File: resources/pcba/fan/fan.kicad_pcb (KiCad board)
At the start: 2 copper layers, 19 x 18 mm, 7 parts, among them Q1 PMOS 9301

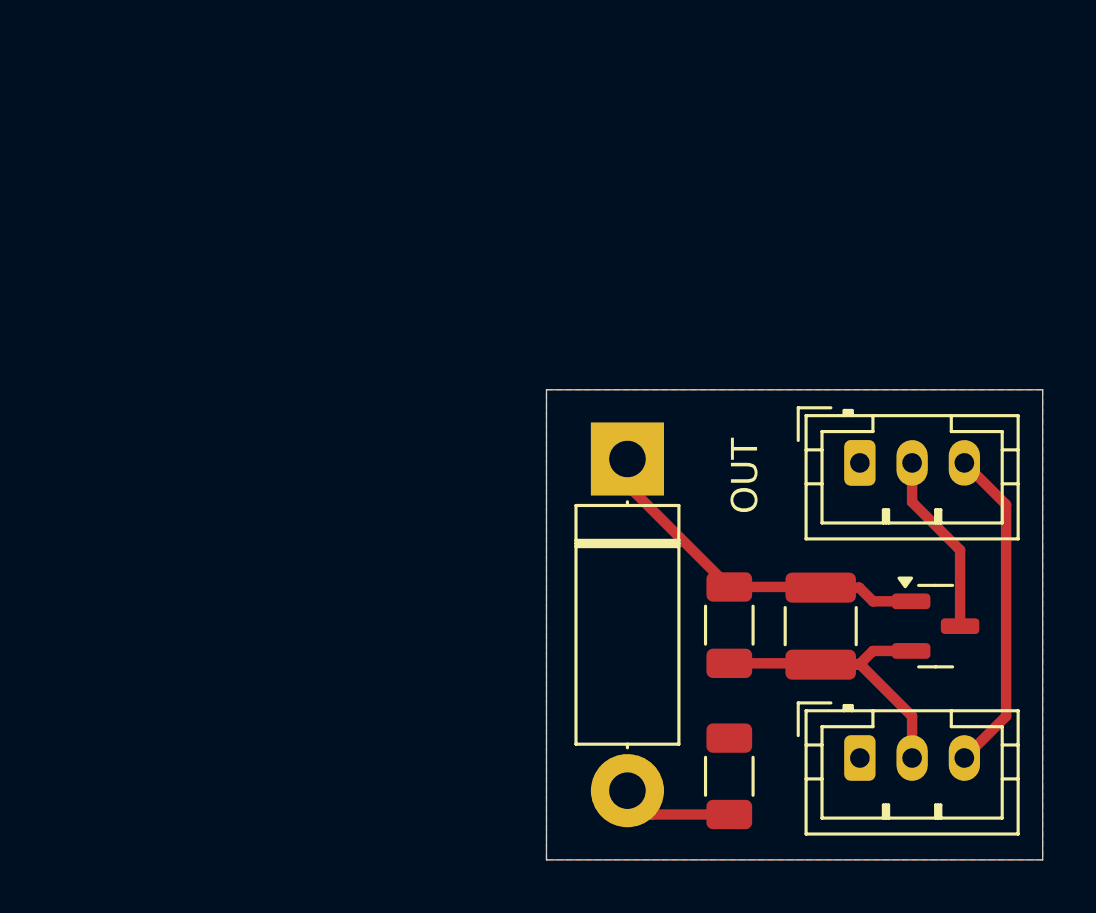
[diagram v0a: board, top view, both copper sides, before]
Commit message: add uvp and fan pcb
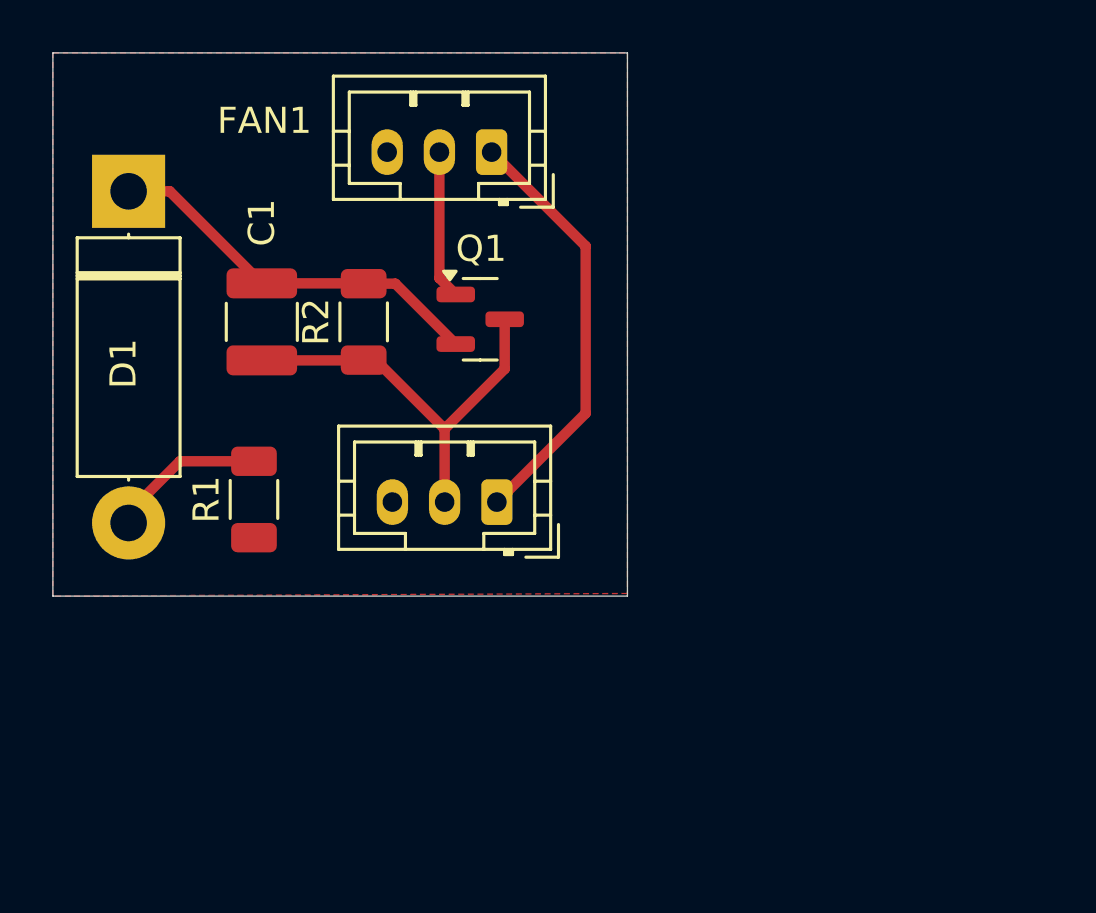
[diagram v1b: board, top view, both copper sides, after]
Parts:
- removed IN1: y1=0 y2=8 td=10m tr=1m tf=1m tw=100n per=10m, Connector_JST:JST_PH_B3B-PH-K_1x03_P2.00mm_Vertical
- removed IN2: OUT, Connector_JST:JST_PH_B3B-PH-K_1x03_P2.00mm_Vertical
- added FAN1: Conn_01x03_Socket, Connector_JST:JST_PH_B3B-PH-K_1x03_P2.00mm_Vertical, F.Cu at (124.9, 64.9)
- added INV1: Conn_01x03_Socket, Connector_JST:JST_PH_B3B-PH-K_1x03_P2.00mm_Vertical, F.Cu at (125.1, 78.3)
- C1: value 22uF -> 10u
- Q1: value PMOS 9301 -> PMOS
- R1: value 10k -> 1k
- R2: value 1k -> 10k
- moved C1 24.4 mm to (116.1, 71.4)
- moved R2 22.3 mm to (120.0, 71.4), turned to 90 degrees
- moved D1 21.7 mm to (111.0, 66.4)
- moved Q1 21.0 mm to (124.5, 71.3)
- moved R1 18.8 mm to (115.8, 78.2), turned to 90 degrees
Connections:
- C1 pad 2: +12V -> Net-(INV1-+)
- Q1 pad 1: Net-(D1-K) -> /FAN
- Q1 pad 2: +12V -> Net-(D1-K)
- Q1 pad 3: /FAN -> Net-(INV1-+)
- R1 pad 1: Net-(D1-K) -> GND
- R1 pad 2: +12V -> Net-(D1-A)
- R2 pad 1: GND -> Net-(INV1-+)
- R2 pad 2: Net-(D1-A) -> Net-(D1-K)
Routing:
- net Net-(INV1-+): track 0.00 -> 16.1 mm
- net +12V: track 13.0 -> 0.00 mm
- net /TACHOMETER: track 12.6 -> 16.3 mm
- net Net-(D1-A): track 4.28 -> 6.01 mm
- net /FAN: track 7.01 -> 5.71 mm
- net Net-(D1-K): track 13.8 -> 14.9 mm
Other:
- board size 19 x 18 mm -> 22 x 20.8 mm
